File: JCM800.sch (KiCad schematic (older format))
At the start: 75 parts, among them U1 ECC83, U2 ECC83, U3 EL84

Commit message: Preparing v0.2
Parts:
- R11: footprint Resistor_THT:R_Axial_DIN0411_L9.9mm_D3.6mm_P15.24mm_Horizontal -> Resistor_THT:R_Axial_DIN0414_L11.9mm_D4.5mm_P15.24mm_Horizontal
- R13: footprint Resistor_THT:R_Axial_DIN0411_L9.9mm_D3.6mm_P15.24mm_Horizontal -> Resistor_THT:R_Axial_DIN0617_L17.0mm_D6.0mm_P25.40mm_Horizontal
- R8: footprint Resistor_THT:R_Axial_DIN0207_L6.3mm_D2.5mm_P10.16mm_Horizontal -> Resistor_THT:R_Axial_DIN0414_L11.9mm_D4.5mm_P15.24mm_Horizontal
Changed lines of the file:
@@
 Title "JCM800 6W"
 Date ""
-Rev "0.1"
+Rev "0.2"
 Comp "Dazz"
 Comment1 ""
@@
 F 0 "R13" V 7243 2950 50  0000 C CNN
 F 1 "4K7/3W" V 7334 2950 50  0000 C CNN
-F 2 "Resistor_THT:R_Axial_DIN0411_L9.9mm_D3.6mm_P15.24mm_Horizontal" V 7380 2950 50  0001 C CNN
+F 2 "Resistor_THT:R_Axial_DIN0617_L17.0mm_D6.0mm_P25.40mm_Horizontal" V 7380 2950 50  0001 C CNN
 F 3 "~" H 7450 2950 50  0001 C CNN
 	1    7450 2950
@@
 F 0 "R11" V 6543 2950 50  0000 C CNN
 F 1 "220R/2W" V 6634 2950 50  0000 C CNN
-F 2 "Resistor_THT:R_Axial_DIN0411_L9.9mm_D3.6mm_P15.24mm_Horizontal" V 6680 2950 50  0001 C CNN
+F 2 "Resistor_THT:R_Axial_DIN0414_L11.9mm_D4.5mm_P15.24mm_Horizontal" V 6680 2950 50  0001 C CNN
 F 3 "~" H 6750 2950 50  0001 C CNN
 	1    6750 2950
@@
 F 0 "R8" H 5880 3404 50  0000 R CNN
 F 1 "220K" H 5880 3495 50  0000 R CNN
-F 2 "Resistor_THT:R_Axial_DIN0207_L6.3mm_D2.5mm_P10.16mm_Horizontal" V 5880 3450 50  0001 C CNN
+F 2 "Resistor_THT:R_Axial_DIN0414_L11.9mm_D4.5mm_P15.24mm_Horizontal" V 5880 3450 50  0001 C CNN
 F 3 "~" H 5950 3450 50  0001 C CNN
 	1    5950 3450

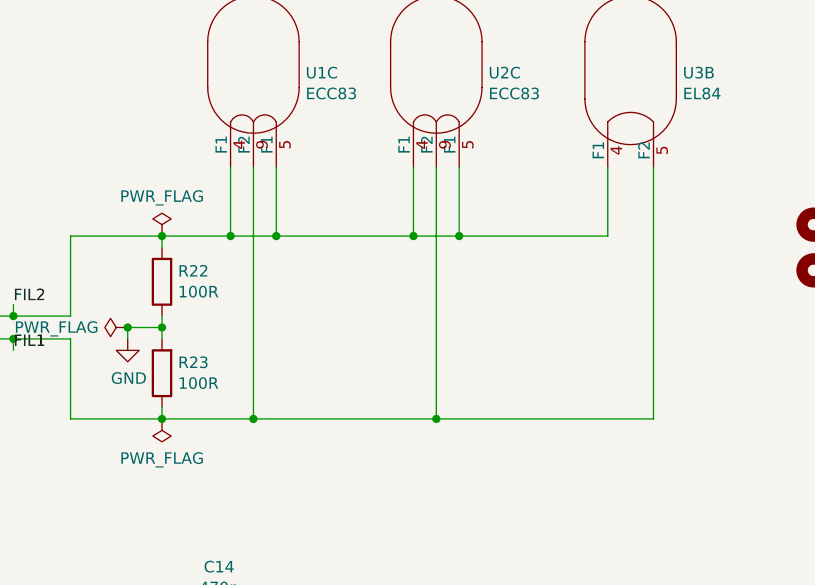
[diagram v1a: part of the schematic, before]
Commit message: 12.6V branch creation.
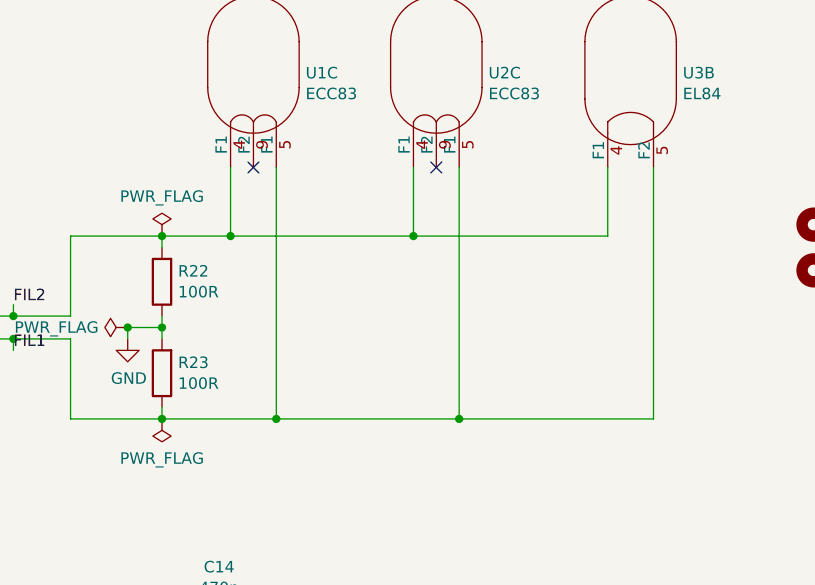
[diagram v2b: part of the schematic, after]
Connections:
- net FIL1: now also U1.5 (F1), U2.5 (F1); no longer U1.9 (F2), U2.9 (F2)
- net FIL2: no longer U1.5 (F1), U2.5 (F1)
- no-connect marks 3 -> 5
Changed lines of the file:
@@
 	8850 2950 8850 4750
 Connection ~ 8850 4750
-Wire Wire Line
-	10450 3800 10650 3800
-Wire Wire Line
-	11250 3800 11450 3800
-Wire Wire Line
-	10650 3800 11250 3800
-Connection ~ 10650 3800
 Connection ~ 11250 3800
-Wire Wire Line
-	11450 3800 12100 3800
-Connection ~ 11450 3800
-Wire Wire Line
-	10550 4600 11350 4600
-Connection ~ 11350 4600
-Wire Wire Line
-	11350 4600 12300 4600
 Wire Wire Line
 	9750 3800 10150 3800
 Connection ~ 10450 3800
-Connection ~ 10550 4600
 Wire Wire Line
 	10450 3500 10450 3800
 Wire Wire Line
-	10650 3500 10650 3800
-Wire Wire Line
 	11250 3500 11250 3800
-Wire Wire Line
-	11450 3500 11450 3800
 Wire Wire Line
 	12100 3500 12100 3800
@@
 $EndComp
 Wire Wire Line
-	10550 3500 10550 4600
-Wire Wire Line
-	11350 3500 11350 4600
-Wire Wire Line
 	12300 3500 12300 4600
 Wire Wire Line
@@
 	10150 4550 10150 4600
 Connection ~ 10150 4600
-Wire Wire Line
-	10150 4600 10550 4600
 Wire Wire Line
 	10150 4250 10150 4200
@@
 	11700 6300 12100 6300
 Connection ~ 12100 6300
+Wire Wire Line
+	10150 4600 10650 4600
+Wire Wire Line
+	10450 3800 11250 3800
+Wire Wire Line
+	11250 3800 12100 3800
+Wire Wire Line
+	10650 3500 10650 4600
+Connection ~ 10650 4600
+Wire Wire Line
+	10650 4600 11450 4600
+Wire Wire Line
+	11450 3500 11450 4600
+Connection ~ 11450 4600
+Wire Wire Line
+	11450 4600 12300 4600
+NoConn ~ 11350 3500
+NoConn ~ 10550 3500
 $EndSCHEMATC

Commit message: Tweaks
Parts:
- C16: footprint Capacitor_THT:CP_Radial_D8.0mm_P5.00mm -> Capacitor_THT:CP_Radial_D5.0mm_P2.50mm
- R20: footprint Resistor_THT:R_Axial_DIN0411_L9.9mm_D3.6mm_P15.24mm_Horizontal -> Resistor_THT:R_Axial_DIN0414_L11.9mm_D4.5mm_P15.24mm_Horizontal
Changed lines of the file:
@@
 EESchema Schematic File Version 4
-LIBS:JCM800-cache
 EELAYER 30 0
 EELAYER END
@@
 F 0 "C16" H 13818 7246 50  0000 L CNN
 F 1 "22u" H 13818 7155 50  0000 L CNN
-F 2 "Capacitor_THT:CP_Radial_D8.0mm_P5.00mm" H 13738 7050 50  0001 C CNN
+F 2 "Capacitor_THT:CP_Radial_D5.0mm_P2.50mm" H 13738 7050 50  0001 C CNN
 F 3 "~" H 13700 7200 50  0001 C CNN
 	1    13700 7200
@@
 F 0 "R20" H 13080 7154 50  0000 R CNN
 F 1 "220R" H 13080 7245 50  0000 R CNN
-F 2 "Resistor_THT:R_Axial_DIN0411_L9.9mm_D3.6mm_P15.24mm_Horizontal" V 13080 7200 50  0001 C CNN
+F 2 "Resistor_THT:R_Axial_DIN0414_L11.9mm_D4.5mm_P15.24mm_Horizontal" V 13080 7200 50  0001 C CNN
 F 3 "~" H 13150 7200 50  0001 C CNN
 	1    13150 7200

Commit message: Push-Pull branch
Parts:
- removed B1: B1, Connector_PinHeader_2.54mm:PinHeader_1x01_P2.54mm_Vertical, symbol Connector:Conn_01x01_Male
- removed C16: 22u, Capacitor_THT:CP_Radial_D5.0mm_P2.50mm, symbol Device:CP
- removed PRESENCE1: PRESENCE, TerminalBlock_MetzConnect:TerminalBlock_MetzConnect_Type094_RT03502HBLU_1x02_P5.00mm_Horizontal, symbol Connector:Conn_01x02_Male
- added C16, C18, C19: 22n, Capacitor_THT:C_Rect_L10.3mm_W5.0mm_P7.50mm_MKS4, symbol Device:C
- added C20: 47u, Capacitor_THT:CP_Radial_D7.5mm_P2.50mm, symbol Device:CP
- added C21: 100n, Capacitor_THT:C_Rect_L10.3mm_W5.0mm_P7.50mm_MKS4, symbol Device:C
- added NFB1: B100K, Potentiometer_THT:Potentiometer_Piher_T-16H_Single_Horizontal, symbol Device:R_POT
- added OUT2: OUT2, Connector_PinHeader_2.54mm:PinHeader_1x01_P2.54mm_Vertical, symbol Connector:Conn_01x01_Male
- added PRESENCE1: C22K, Potentiometer_THT:Potentiometer_Piher_T-16H_Single_Horizontal, symbol Device:R_POT
- added R26, R27: 1M, Resistor_THT:R_Axial_DIN0207_L6.3mm_D2.5mm_P10.16mm_Horizontal, symbol Device:R
- added R28, R29: 100K, Resistor_THT:R_Axial_DIN0207_L6.3mm_D2.5mm_P10.16mm_Horizontal, symbol Device:R
- added R30, R31: 470K, Resistor_THT:R_Axial_DIN0207_L6.3mm_D2.5mm_P10.16mm_Horizontal, symbol Device:R
- added R32, R33: 8K2, Resistor_THT:R_Axial_DIN0207_L6.3mm_D2.5mm_P10.16mm_Horizontal, symbol Device:R
- added R34, R35: 100, Resistor_THT:R_Axial_DIN0207_L6.3mm_D2.5mm_P10.16mm_Horizontal, symbol Device:R
- added R36, R37: 4K7, Resistor_THT:R_Axial_DIN0207_L6.3mm_D2.5mm_P10.16mm_Horizontal, symbol Device:R
- added Rbias1: 180, Resistor_THT:R_Axial_DIN0207_L6.3mm_D2.5mm_P10.16mm_Horizontal, symbol Device:R
- added U3: ECC83, tubes:NOVAL, symbol Valve:ECC83
- added U5: EL84, tubes:NOVAL, symbol Valve:EL84
- C17: value 22n -> 100n
- LEVEL1: value A1M -> A50K
- OUT1: value OUT -> OUT1
- R11: value 220R/2W -> 2K2-2W
- R13: value 4K7/3W -> 8K2-1W; footprint Resistor_THT:R_Axial_DIN0617_L17.0mm_D6.0mm_P25.40mm_Horizontal -> Resistor_THT:R_Axial_DIN0414_L11.9mm_D4.5mm_P15.24mm_Horizontal
- R19: value 10K -> ?K
- R20: value 220R -> 10K; footprint Resistor_THT:R_Axial_DIN0414_L11.9mm_D4.5mm_P15.24mm_Horizontal -> Resistor_THT:R_Axial_DIN0207_L6.3mm_D2.5mm_P10.16mm_Horizontal
- R21: value 1K -> 470
- renumbered U3 to U4
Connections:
- net FIL1: now also U3.5 (F1), U5.5 (F2)
- net FIL2: now also U3.4 (F1), U5.4 (F1)
- net GND: now also C20.2, PRESENCE1.1, PRESENCE1.2, R30.2, R31.1, R36.2, Rbias1.2; no longer R20.1
- net NFB: now reaches C17.2
- net NFB: now also R20.1, C21.2, R36.1, R37.2
- net at TREBLE1.2: now also R19.2; no longer LEVEL1.3
- net at R19.1: now also LEVEL1.3; no longer U4.2 (G1)
- net at U4.9 (G2): now also R34.1; no longer R21.2
- net A1 renamed E
- net A2 renamed D
- net B1 renamed B
- net B: now also R34.2, R35.1
- net B2 renamed C
- net C: now also R28.2, R29.1; no longer R21.1
- net EL84-CATHODE: no longer names the net of U4.3 (K_G3)
- net EL84-CATHODE: now also C20.1, Rbias1.1, U5.3 (K_G3); no longer R20.2
- net OUT renamed OUT1
- net RECTF renamed A
- new net: R32.1, U4.2 (G1)
- new net: C18.2, R28.1, U3.1 (A)
- new net: C16.1, R26.1, U3.2 (G)
- new net: R21.2, U3.3 (K), U3.8 (K)
- new net: C19.2, R29.2, U3.6 (A)
- new net: C17.1, R27.2, U3.7 (G)
- new net: R20.2, R21.1, R26.2, R27.1
- new net: C18.1, R30.1, R32.2
- new net: C19.1, R31.2, R33.2
- new net: R33.1, U5.2 (G1)
- new net: R35.2, U5.9 (G2)
- new net: C21.1, PRESENCE1.3
- new net: NFB1.1, R37.1
- new net 4ohm: NFB1.2, NFB1.3
- new net OUT2: OUT2.1 (Pin_1), U5.7 (A)
- new net TO_PA: C16.2, LEVEL1.2
- no-connect marks 5 -> 6
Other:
- moved on the sheet: AC1, BASS1, C1, C10, C11, C12, C13, C14, C15, C2, C3, C4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

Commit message: .
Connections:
- net FIL1: now also FIL1.2 (Pin_2); no longer FIL1.1 (Pin_1), U4.5 (F2)
- net FIL2: now also FIL1.1 (Pin_1); no longer FIL1.2 (Pin_2), U5.4 (F1)
- new net: U4.5 (F2), U5.4 (F1)
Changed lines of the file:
@@
 $EndComp
-Wire Wire Line
-	13450 1800 13450 2900
 Wire Wire Line
 	10450 2150 10450 2100
@@
 L Connector:Conn_01x02_Male FIL1
 U 1 1 5DC9A7F9
-P 9450 2550
-F 0 "FIL1" H 9558 2731 50  0000 C CNN
-F 1 "FIL" H 9558 2640 50  0000 C CNN
-F 2 "TerminalBlock_MetzConnect:TerminalBlock_MetzConnect_Type094_RT03502HBLU_1x02_P5.00mm_Horizontal" H 9450 2550 50  0001 C CNN
-F 3 "~" H 9450 2550 50  0001 C CNN
-	1    9450 2550
-	1    0    0    1
+P 9450 2450
+F 0 "FIL1" H 9558 2631 50  0000 C CNN
+F 1 "FIL" H 9558 2540 50  0000 C CNN
+F 2 "TerminalBlock_MetzConnect:TerminalBlock_MetzConnect_Type094_RT03502HBLU_1x02_P5.00mm_Horizontal" H 9450 2450 50  0001 C CNN
+F 3 "~" H 9450 2450 50  0001 C CNN
+	1    9450 2450
+	1    0    0    -1
 $EndComp
 Wire Wire Line
@@
 	12400 1800 12400 2100
 Wire Wire Line
-	14100 1800 14100 2100
-Wire Wire Line
-	14300 1800 14300 2900
-Wire Wire Line
 	12400 2100 13250 2100
 Connection ~ 12400 2100
-Wire Wire Line
-	13450 2900 12600 2900
 Connection ~ 12600 2900
-Wire Wire Line
-	13250 2100 14100 2100
-Connection ~ 13250 2100
-Wire Wire Line
-	13450 2900 14300 2900
-Connection ~ 13450 2900
 $Comp
 L Valve:EL84 U5
@@
 	4950 10200 5150 10200
 NoConn ~ 12500 1800
+Wire Wire Line
+	12600 2900 14300 2900
+Wire Wire Line
+	14300 1800 14300 2900
+Wire Wire Line
+	13450 2100 13800 2100
+Wire Wire Line
+	14100 2100 14100 1800
+Wire Wire Line
+	13450 1800 13450 2100
+$Comp
+L power:PWR_FLAG #FLG0106
+U 1 1 5DEB167B
+P 13800 2100
+F 0 "#FLG0106" H 13800 2175 50  0001 C CNN
+F 1 "PWR_FLAG" H 13800 2273 50  0000 C CNN
+F 2 "" H 13800 2100 50  0001 C CNN
+F 3 "~" H 13800 2100 50  0001 C CNN
+	1    13800 2100
+	1    0    0    -1
+$EndComp
+Connection ~ 13800 2100
+Wire Wire Line
+	13800 2100 14100 2100
 $EndSCHEMATC

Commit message: Preparing initial release
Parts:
- added H10, H11, H8, H9: MountingHole, MountingHole:MountingHole_3.2mm_M3, symbol Mechanical:MountingHole
- R11: footprint Resistor_THT:R_Axial_DIN0414_L11.9mm_D4.5mm_P15.24mm_Horizontal -> Resistor_THT:R_Axial_DIN0516_L15.5mm_D5.0mm_P20.32mm_Horizontal
- Rbias1: footprint Resistor_THT:R_Axial_DIN0207_L6.3mm_D2.5mm_P10.16mm_Horizontal -> Resistor_THT:R_Axial_DIN0414_L11.9mm_D4.5mm_P15.24mm_Horizontal
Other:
- moved on the sheet: H4, H5, H6, H7
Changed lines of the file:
@@
 encoding utf-8
 Sheet 1 1
-Title "JCM800 6W"
+Title "JCM800 15W"
 Date ""
-Rev "0.2"
+Rev "0.1"
 Comp "Dazz"
 Comment1 ""
@@
 F 0 "R11" V 6493 1250 50  0000 C CNN
 F 1 "2K2-2W" V 6584 1250 50  0000 C CNN
-F 2 "Resistor_THT:R_Axial_DIN0414_L11.9mm_D4.5mm_P15.24mm_Horizontal" V 6630 1250 50  0001 C CNN
+F 2 "Resistor_THT:R_Axial_DIN0516_L15.5mm_D5.0mm_P20.32mm_Horizontal" V 6630 1250 50  0001 C CNN
 F 3 "~" H 6700 1250 50  0001 C CNN
 	1    6700 1250
@@
 L Mechanical:MountingHole H4
 U 1 1 5DBB9A75
+P 13850 3700
+F 0 "H4" H 13950 3746 50  0000 L CNN
+F 1 "MountingHole" H 13950 3655 50  0000 L CNN
+F 2 "MountingHole:MountingHole_3.2mm_M3" H 13850 3700 50  0001 C CNN
+F 3 "~" H 13850 3700 50  0001 C CNN
+	1    13850 3700
+	1    0    0    -1
+$EndComp
+$Comp
+L Mechanical:MountingHole H5
+U 1 1 5DBB9EB7
 P 12950 3900
-F 0 "H4" H 13050 3946 50  0000 L CNN
+F 0 "H5" H 13050 3946 50  0000 L CNN
 F 1 "MountingHole" H 13050 3855 50  0000 L CNN
 F 2 "MountingHole:MountingHole_3.2mm_M3" H 12950 3900 50  0001 C CNN
@@
 $EndComp
 $Comp
-L Mechanical:MountingHole H5
-U 1 1 5DBB9EB7
+L Mechanical:MountingHole H6
+U 1 1 5DBBA083
 P 13250 3900
-F 0 "H5" H 13350 3946 50  0000 L CNN
+F 0 "H6" H 13350 3946 50  0000 L CNN
 F 1 "MountingHole" H 13350 3855 50  0000 L CNN
 F 2 "MountingHole:MountingHole_3.2mm_M3" H 13250 3900 50  0001 C CNN
@@
 $EndComp
 $Comp
-L Mechanical:MountingHole H6
-U 1 1 5DBBA083
+L Mechanical:MountingHole H7
+U 1 1 5DBBA434
 P 13550 3900
-F 0 "H6" H 13650 3946 50  0000 L CNN
+F 0 "H7" H 13650 3946 50  0000 L CNN
 F 1 "MountingHole" H 13650 3855 50  0000 L CNN
 F 2 "MountingHole:MountingHole_3.2mm_M3" H 13550 3900 50  0001 C CNN
 F 3 "~" H 13550 3900 50  0001 C CNN
 	1    13550 3900
-	1    0    0    -1
-$EndComp
-$Comp
-L Mechanical:MountingHole H7
-U 1 1 5DBBA434
-P 13800 3900
-F 0 "H7" H 13900 3946 50  0000 L CNN
-F 1 "MountingHole" H 13900 3855 50  0000 L CNN
-F 2 "MountingHole:MountingHole_3.2mm_M3" H 13800 3900 50  0001 C CNN
-F 3 "~" H 13800 3900 50  0001 C CNN
-	1    13800 3900
 	1    0    0    -1
 $EndComp
@@
 F 0 "Rbias1" V 8093 8150 50  0000 C CNN
 F 1 "180" V 8184 8150 50  0000 C CNN
-F 2 "Resistor_THT:R_Axial_DIN0207_L6.3mm_D2.5mm_P10.16mm_Horizontal" V 8230 8150 50  0001 C CNN
+F 2 "Resistor_THT:R_Axial_DIN0414_L11.9mm_D4.5mm_P15.24mm_Horizontal" V 8230 8150 50  0001 C CNN
 F 3 "~" H 8300 8150 50  0001 C CNN
 	1    8300 8150
@@
 Wire Wire Line
 	13800 2100 14100 2100
+$Comp
+L Mechanical:MountingHole H8
+U 1 1 5E00F48C
+P 13850 3900
+F 0 "H8" H 13950 3946 50  0000 L CNN
+F 1 "MountingHole" H 13950 3855 50  0000 L CNN
+F 2 "MountingHole:MountingHole_3.2mm_M3" H 13850 3900 50  0001 C CNN
+F 3 "~" H 13850 3900 50  0001 C CNN
+	1    13850 3900
+	1    0    0    -1
+$EndComp
+$Comp
+L Mechanical:MountingHole H9
+U 1 1 5E0BFD3C
+P 14200 3900
+F 0 "H9" H 14300 3946 50  0000 L CNN
+F 1 "MountingHole" H 14300 3855 50  0000 L CNN
+F 2 "MountingHole:MountingHole_3.2mm_M3" H 14200 3900 50  0001 C CNN
+F 3 "~" H 14200 3900 50  0001 C CNN
+	1    14200 3900
+	1    0    0    -1
+$EndComp
+$Comp
+L Mechanical:MountingHole H10
+U 1 1 5E0BFD42
+P 14500 3900
+F 0 "H10" H 14600 3946 50  0000 L CNN
+F 1 "MountingHole" H 14600 3855 50  0000 L CNN
+F 2 "MountingHole:MountingHole_3.2mm_M3" H 14500 3900 50  0001 C CNN
+F 3 "~" H 14500 3900 50  0001 C CNN
+	1    14500 3900
+	1    0    0    -1
+$EndComp
+$Comp
+L Mechanical:MountingHole H11
+U 1 1 5E0BFD48
+P 14800 3900
+F 0 "H11" H 14900 3946 50  0000 L CNN
+F 1 "MountingHole" H 14900 3855 50  0000 L CNN
+F 2 "MountingHole:MountingHole_3.2mm_M3" H 14800 3900 50  0001 C CNN
+F 3 "~" H 14800 3900 50  0001 C CNN
+	1    14800 3900
+	1    0    0    -1
+$EndComp
 $EndSCHEMATC

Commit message: Preparing initial release
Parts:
- added BOOST1: BOOST, TerminalBlock_MetzConnect:TerminalBlock_MetzConnect_Type094_RT03502HBLU_1x02_P5.00mm_Horizontal, symbol Connector:Conn_01x02_Male
- added C22: 1n, Capacitor_THT:C_Rect_L7.0mm_W3.5mm_P5.00mm, symbol Device:C
- added NFB2: 4ohm, Connector_PinHeader_2.54mm:PinHeader_1x01_P2.54mm_Vertical, symbol Connector:Conn_01x01_Male
- R37: value 4K7 -> 47K
- Rbias1: value 180 -> 180R-2W
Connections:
- net 4ohm: now also NFB2.1 (Pin_1)
- net GND: now also C22.2
- net at R6.2, U1.8 (K): now also BOOST1.1 (Pin_1)
- new net: BOOST1.2 (Pin_2), C22.1
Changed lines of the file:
@@
 $EndComp
-Wire Wire Line
-	5700 5550 5700 5450
 Wire Wire Line
 	5700 5850 5700 5950
@@
 $EndComp
 $Comp
-L Valve:ECC83 U1
-U 1 1 5DB3562C
-P 5800 5050
-F 0 "U1" H 6028 5096 50  0000 L CNN
-F 1 "ECC83" H 6028 5005 50  0000 L CNN
-F 2 "tubes:NOVAL" H 6070 4650 50  0001 C CNN
-F 3 "http://www.r-type.org/pdfs/ecc83.pdf" H 5800 5050 50  0001 C CNN
-	1    5800 5050
-	1    0    0    -1
-$EndComp
-$Comp
 L Connector:AudioJack2_Switch IN_LOW_1
 U 1 1 5DBA9657
@@
 	8600 7450 8600 8150
 $Comp
-L Device:R Rbias1
-U 1 1 5E1C5A69
-P 8300 8150
-F 0 "Rbias1" V 8093 8150 50  0000 C CNN
-F 1 "180" V 8184 8150 50  0000 C CNN
-F 2 "Resistor_THT:R_Axial_DIN0414_L11.9mm_D4.5mm_P15.24mm_Horizontal" V 8230 8150 50  0001 C CNN
-F 3 "~" H 8300 8150 50  0001 C CNN
-	1    8300 8150
-	0    1    1    0
-$EndComp
-$Comp
 L Device:CP C20
 U 1 1 5E1C61A4
@@
 Wire Wire Line
 	3650 10150 3650 9850
-$Comp
-L Device:R R37
-U 1 1 5E3FFE1A
-P 4650 9850
-F 0 "R37" V 4443 9850 50  0000 C CNN
-F 1 "4K7" V 4534 9850 50  0000 C CNN
-F 2 "Resistor_THT:R_Axial_DIN0207_L6.3mm_D2.5mm_P10.16mm_Horizontal" V 4580 9850 50  0001 C CNN
-F 3 "~" H 4650 9850 50  0001 C CNN
-	1    4650 9850
-	0    1    1    0
-$EndComp
 Wire Wire Line
 	4350 9850 4500 9850
@@
 	1    0    0    -1
 $EndComp
+$Comp
+L Device:C C22
+U 1 1 5E201D83
+P 6050 5700
+F 0 "C22" H 6165 5746 50  0000 L CNN
+F 1 "1n" H 6165 5655 50  0000 L CNN
+F 2 "Capacitor_THT:C_Rect_L7.0mm_W3.5mm_P5.00mm" H 6088 5550 50  0001 C CNN
+F 3 "~" H 6050 5700 50  0001 C CNN
+	1    6050 5700
+	1    0    0    -1
+$EndComp
+$Comp
+L power:GND #PWR0107
+U 1 1 5E24F6B8
+P 6050 5950
+F 0 "#PWR0107" H 6050 5700 50  0001 C CNN
+F 1 "GND" H 6055 5777 50  0000 C CNN
+F 2 "" H 6050 5950 50  0001 C CNN
+F 3 "" H 6050 5950 50  0001 C CNN
+	1    6050 5950
+	1    0    0    -1
+$EndComp
+Wire Wire Line
+	6050 5950 6050 5850
+Wire Wire Line
+	5700 5450 5700 5550
+Wire Wire Line
+	5950 5550 5700 5550
+Connection ~ 5700 5550
+$Comp
+L Connector:Conn_01x02_Male BOOST1
+U 1 1 5E2A422F
+P 5950 5350
+F 0 "BOOST1" V 6000 5100 50  0000 C CNN
+F 1 "BOOST" V 6100 5100 50  0000 C CNN
+F 2 "TerminalBlock_MetzConnect:TerminalBlock_MetzConnect_Type094_RT03502HBLU_1x02_P5.00mm_Horizontal" H 5950 5350 50  0001 C CNN
+F 3 "~" H 5950 5350 50  0001 C CNN
+	1    5950 5350
+	0    -1   1    0
+$EndComp
+$Comp
+L Valve:ECC83 U1
+U 1 1 5DB3562C
+P 5800 5050
+F 0 "U1" H 6028 5096 50  0000 L CNN
+F 1 "ECC83" H 6028 5005 50  0000 L CNN
+F 2 "tubes:NOVAL" H 6070 4650 50  0001 C CNN
+F 3 "http://www.r-type.org/pdfs/ecc83.pdf" H 5800 5050 50  0001 C CNN
+	1    5800 5050
+	1    0    0    -1
+$EndComp
+$Comp
+L Device:R Rbias1
+U 1 1 5E1C5A69
+P 8300 8150
+F 0 "Rbias1" V 8093 8150 50  0000 C CNN
+F 1 "180R-2W" V 8184 8150 50  0000 C CNN
+F 2 "Resistor_THT:R_Axial_DIN0414_L11.9mm_D4.5mm_P15.24mm_Horizontal" V 8230 8150 50  0001 C CNN
+F 3 "~" H 8300 8150 50  0001 C CNN
+	1    8300 8150
+	0    1    1    0
+$EndComp
+$Comp
+L Connector:Conn_01x01_Male NFB2
+U 1 1 5E38BCC9
+P 5900 10200
+F 0 "NFB2" H 5872 10132 50  0000 R CNN
+F 1 "4ohm" H 5872 10223 50  0000 R CNN
+F 2 "Connector_PinHeader_2.54mm:PinHeader_1x01_P2.54mm_Vertical" H 5900 10200 50  0001 C CNN
+F 3 "~" H 5900 10200 50  0001 C CNN
+	1    5900 10200
+	-1   0    0    1
+$EndComp
+$Comp
+L Device:R R37
+U 1 1 5E3FFE1A
+P 4650 9850
+F 0 "R37" V 4443 9850 50  0000 C CNN
+F 1 "47K" V 4534 9850 50  0000 C CNN
+F 2 "Resistor_THT:R_Axial_DIN0207_L6.3mm_D2.5mm_P10.16mm_Horizontal" V 4580 9850 50  0001 C CNN
+F 3 "~" H 4650 9850 50  0001 C CNN
+	1    4650 9850
+	0    1    1    0
+$EndComp
 $EndSCHEMATC

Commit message: Beef up filter and bias resistors
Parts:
- C22: value 1n -> 1u
- R11: value 2K2-2W -> 2K2/5W; footprint Resistor_THT:R_Axial_DIN0516_L15.5mm_D5.0mm_P20.32mm_Horizontal -> Resistor_THT:R_Axial_DIN0922_L20.0mm_D9.0mm_P7.62mm_Vertical
- R13: value 8K2-1W -> 8K2/2W
- R8: value 220K -> 220K/2W
- Rbias1: value 180R-2W -> 180R/5W; footprint Resistor_THT:R_Axial_DIN0414_L11.9mm_D4.5mm_P15.24mm_Horizontal -> Resistor_THT:R_Axial_DIN0922_L20.0mm_D9.0mm_P7.62mm_Vertical
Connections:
- net A: now also R8.1; no longer R8.2
- net GND: now also R8.2; no longer R8.1
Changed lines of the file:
@@
 P 7400 1250
 F 0 "R13" V 7193 1250 50  0000 C CNN
-F 1 "8K2-1W" V 7284 1250 50  0000 C CNN
+F 1 "8K2/2W" V 7284 1250 50  0000 C CNN
 F 2 "Resistor_THT:R_Axial_DIN0414_L11.9mm_D4.5mm_P15.24mm_Horizontal" V 7330 1250 50  0001 C CNN
 F 3 "~" H 7400 1250 50  0001 C CNN
@@
 P 6700 1250
 F 0 "R11" V 6493 1250 50  0000 C CNN
-F 1 "2K2-2W" V 6584 1250 50  0000 C CNN
-F 2 "Resistor_THT:R_Axial_DIN0516_L15.5mm_D5.0mm_P20.32mm_Horizontal" V 6630 1250 50  0001 C CNN
+F 1 "2K2/5W" V 6584 1250 50  0000 C CNN
+F 2 "Resistor_THT:R_Axial_DIN0922_L20.0mm_D9.0mm_P7.62mm_Vertical" V 6630 1250 50  0001 C CNN
 F 3 "~" H 6700 1250 50  0001 C CNN
 	1    6700 1250
@@
 P 5900 1750
 F 0 "R8" H 5830 1704 50  0000 R CNN
-F 1 "220K" H 5830 1795 50  0000 R CNN
+F 1 "220K/2W" H 5830 1795 50  0000 R CNN
 F 2 "Resistor_THT:R_Axial_DIN0414_L11.9mm_D4.5mm_P15.24mm_Horizontal" V 5830 1750 50  0001 C CNN
 F 3 "~" H 5900 1750 50  0001 C CNN
 	1    5900 1750
-	-1   0    0    1
+	1    0    0    -1
 $EndComp
 $Comp
@@
 P 6050 5700
 F 0 "C22" H 6165 5746 50  0000 L CNN
-F 1 "1n" H 6165 5655 50  0000 L CNN
+F 1 "1u" H 6165 5655 50  0000 L CNN
 F 2 "Capacitor_THT:C_Rect_L7.0mm_W3.5mm_P5.00mm" H 6088 5550 50  0001 C CNN
 F 3 "~" H 6050 5700 50  0001 C CNN
@@
 P 8300 8150
 F 0 "Rbias1" V 8093 8150 50  0000 C CNN
-F 1 "180R-2W" V 8184 8150 50  0000 C CNN
-F 2 "Resistor_THT:R_Axial_DIN0414_L11.9mm_D4.5mm_P15.24mm_Horizontal" V 8230 8150 50  0001 C CNN
+F 1 "180R/5W" V 8184 8150 50  0000 C CNN
+F 2 "Resistor_THT:R_Axial_DIN0922_L20.0mm_D9.0mm_P7.62mm_Vertical" V 8230 8150 50  0001 C CNN
 F 3 "~" H 8300 8150 50  0001 C CNN
 	1    8300 8150
